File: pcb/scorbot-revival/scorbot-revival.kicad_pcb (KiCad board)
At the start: 2 copper layers, 3 parts, among them J1 DB-50, J2 Raspberry_Pi_2_3, U1 L293D

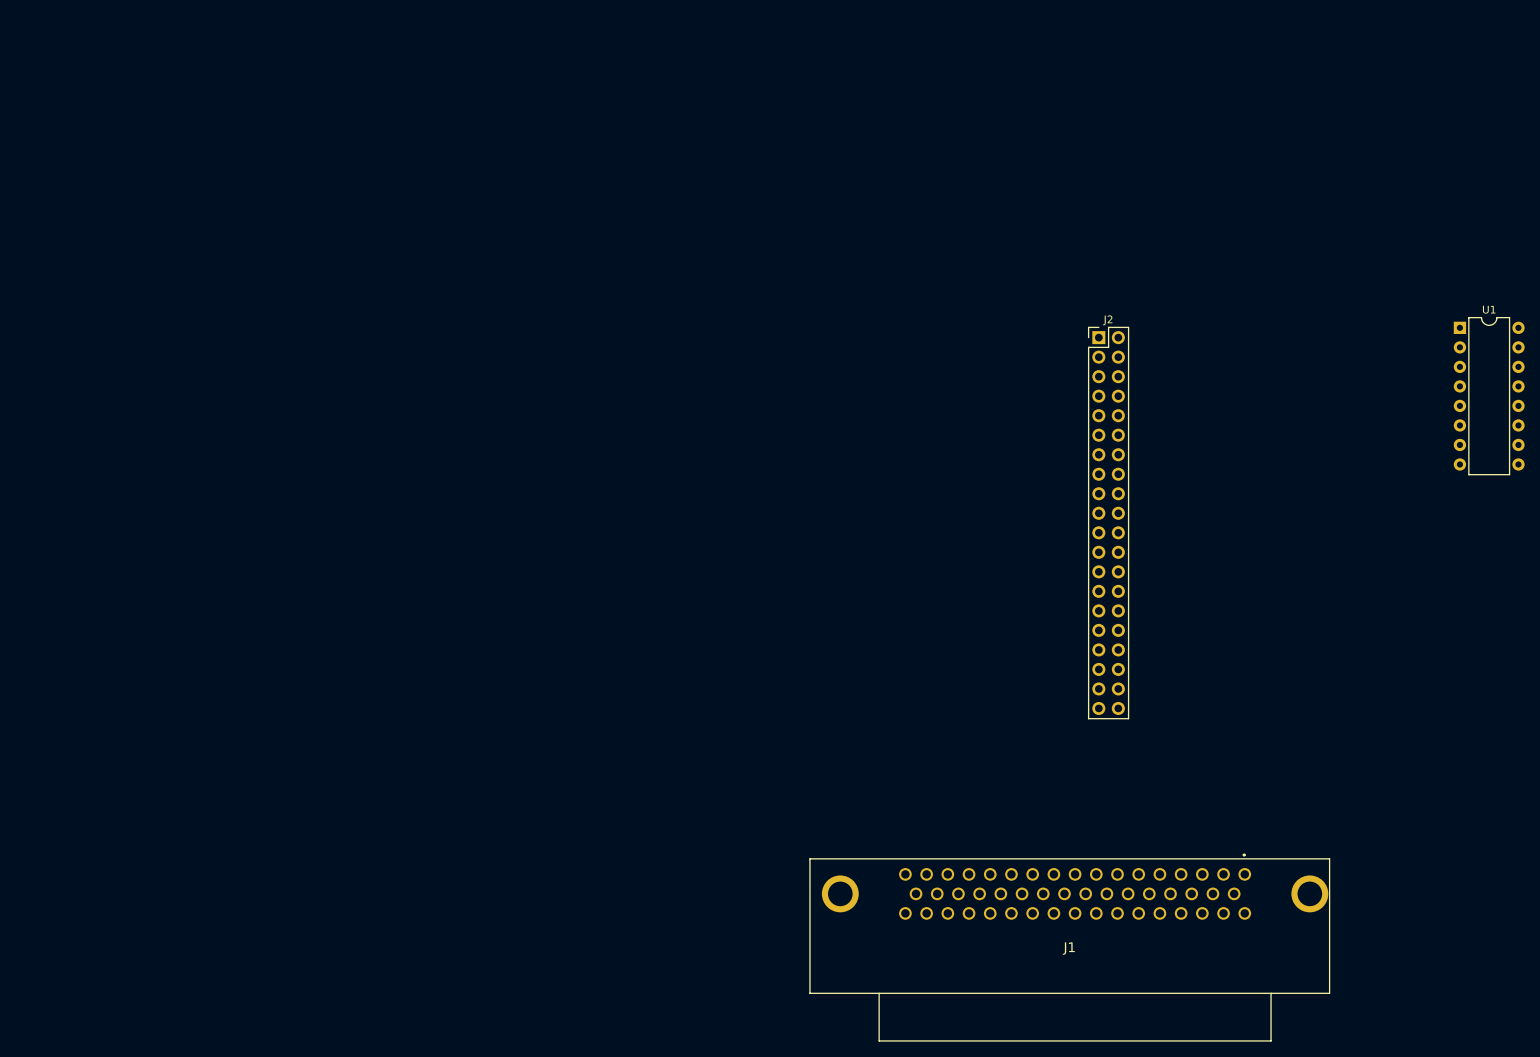
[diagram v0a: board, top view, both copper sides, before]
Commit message: [pcb] added labels to DB50 connector in schematic
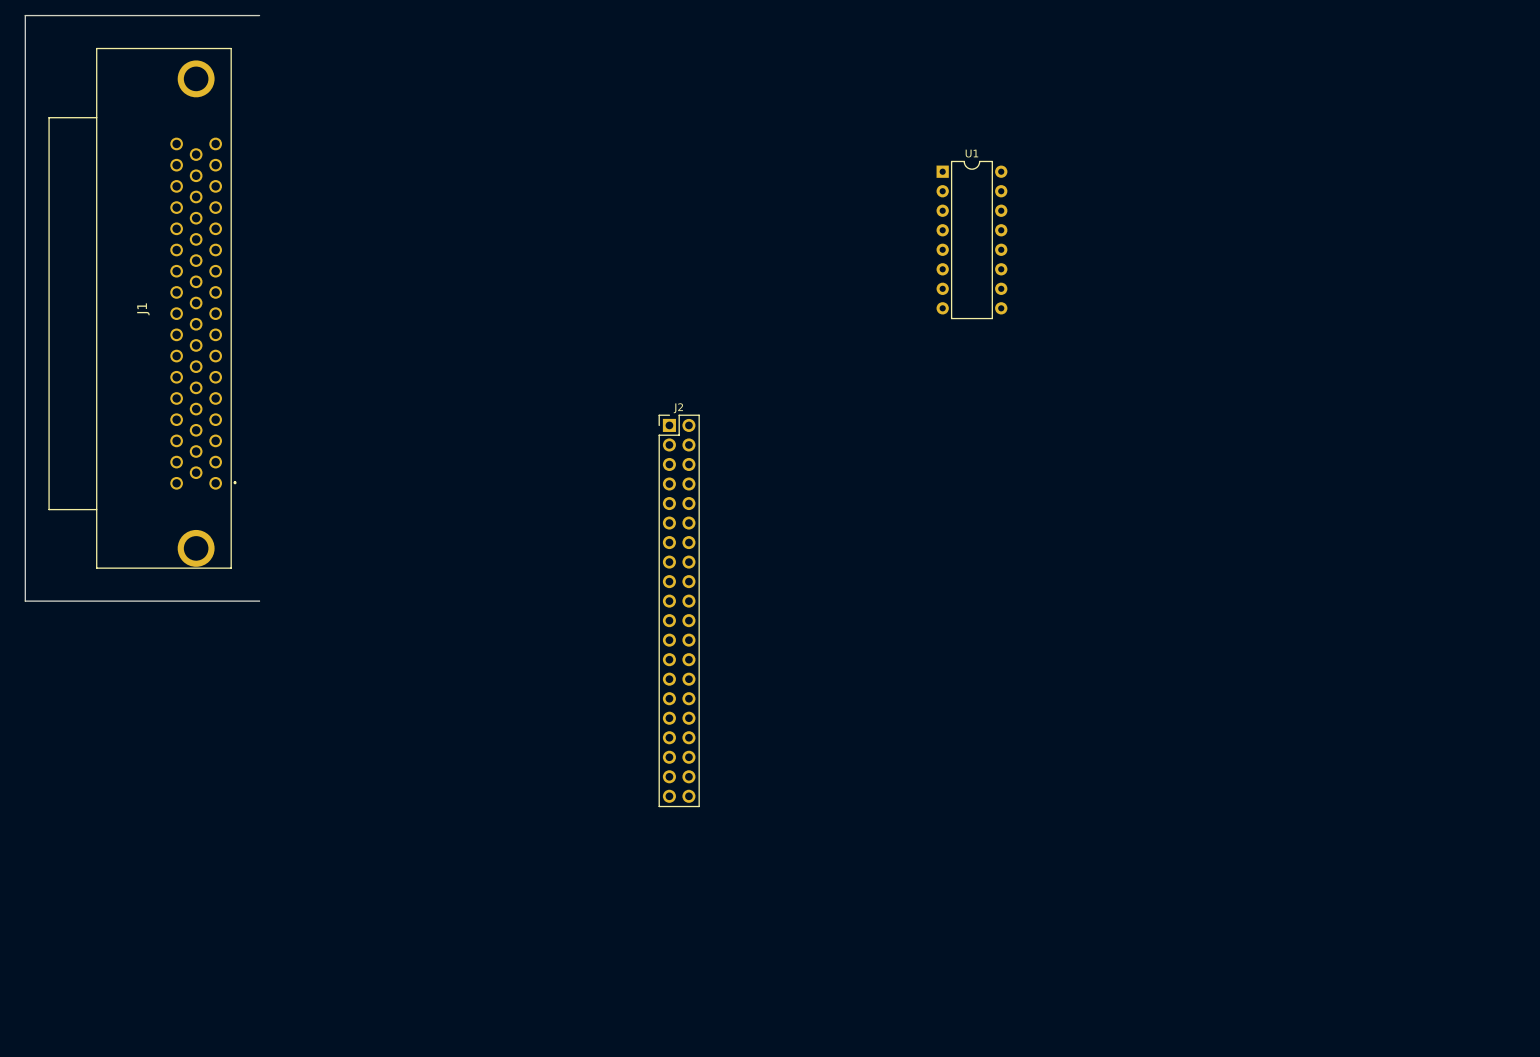
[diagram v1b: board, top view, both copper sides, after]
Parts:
- moved J1 146.6 mm to (35.6, 53.3), turned to 270 degrees
- moved U1 70.3 mm to (139.7, 35.6)
- moved J2 57.0 mm to (104.1, 68.6)
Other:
- board outline added: 30.5 x 76.2 mm

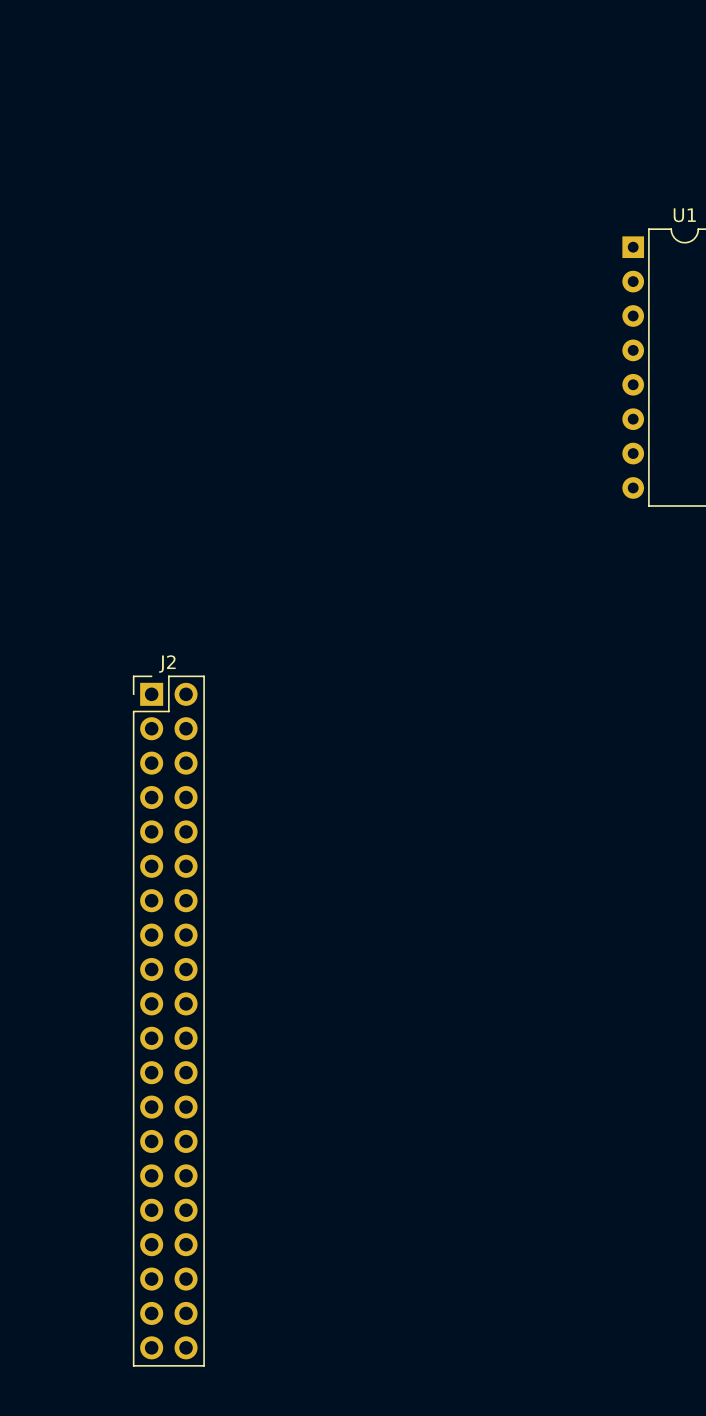
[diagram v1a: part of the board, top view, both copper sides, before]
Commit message: [pcb] add PIC16CE625-04I to schematic + pcbnew
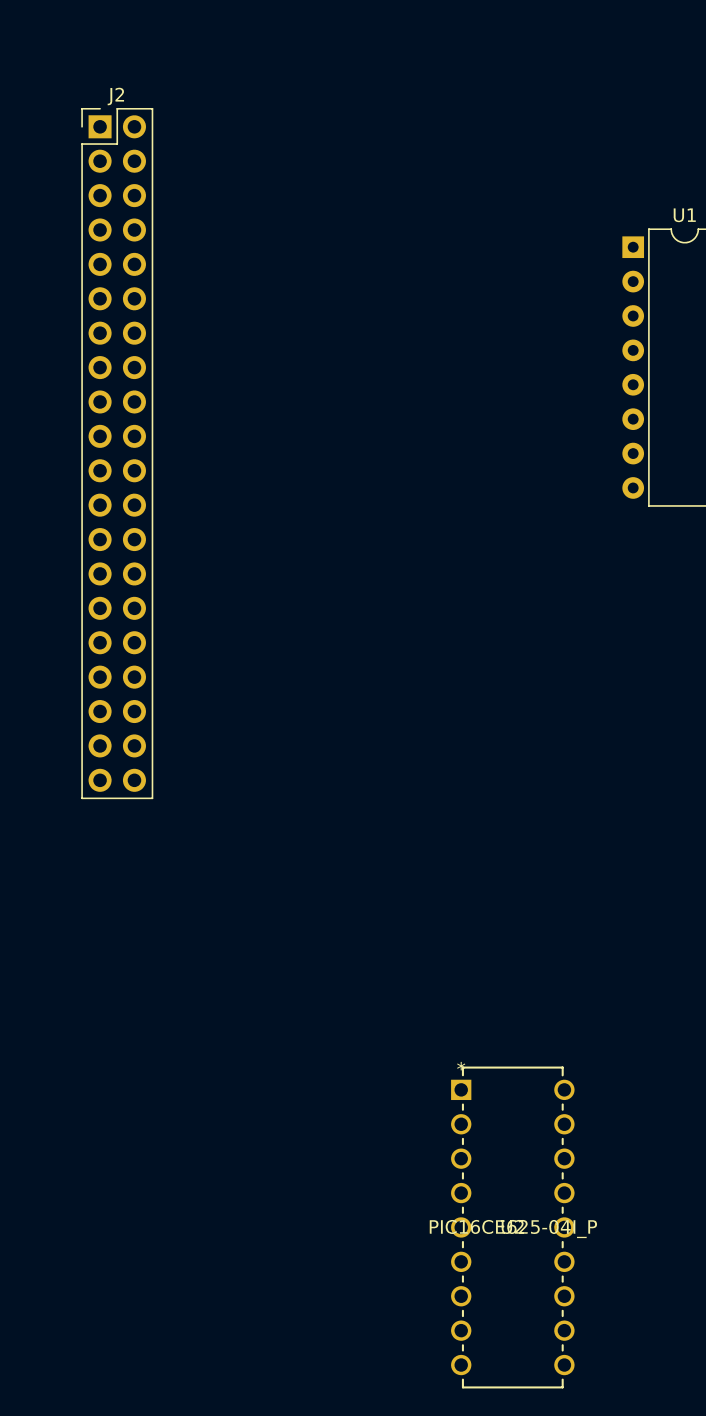
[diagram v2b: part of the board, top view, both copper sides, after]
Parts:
- added U2: PIC16CE625-04I_P, PIC16CE625-04I/P:PIC16CE625-04I&slash_P, F.Cu at (134.6, 118.1)
- moved J2 42.1 mm to (100.3, 26.7)
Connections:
- net Net-(J1-Pad1) renamed /M2_LOGIC_P0
- net Net-(J1-Pad10) renamed /M3_LOGIC_LED
- net Net-(J1-Pad11) renamed /M1_LOGIC_LED
- net Net-(J1-Pad12) renamed /Grp+
- net Net-(J1-Pad13) renamed /M5+
- net Net-(J1-Pad14) renamed /M4+
- net Net-(J1-Pad15) renamed /M3+
- net Net-(J1-Pad16) renamed /M2+
- net Net-(J1-Pad17) renamed /M1+
- net Net-(J1-Pad18) renamed /M5_LOGIC_P0
- net Net-(J1-Pad19) renamed /Grp_LOGIC_P1
- net Net-(J1-Pad2) renamed /M1_LOGIC_P0
- net Net-(J1-Pad20) renamed /M4_LOGIC_P1
- net Net-(J1-Pad21) renamed /M2_LOGIC_P1
- net Net-(J1-Pad22) renamed /Grp_LOGIC_MS
- net Net-(J1-Pad23) renamed /M1_LOGIC_MS
- net Net-(J1-Pad24) renamed /M3_LOGIC_MS
- net Net-(J1-Pad25) renamed /Grp_LOGIC_LED
- net Net-(J1-Pad26) renamed /M4_LOGIC_LED
- net Net-(J1-Pad27) renamed /M2_LOGIC_LED
- net Net-(J1-Pad3) renamed /M5_LOGIC_P1
- net Net-(J1-Pad34) renamed /Grp_LOGIC_P0
- net Net-(J1-Pad35) renamed /M4_LOGIC_P0
- net Net-(J1-Pad36) renamed /M3_LOGIC_P0
- net Net-(J1-Pad4) renamed /M3_LOGIC_P1
- net Net-(J1-Pad45) renamed /Grp-
- net Net-(J1-Pad46) renamed /M5-
- net Net-(J1-Pad47) renamed /M4-
- net Net-(J1-Pad48) renamed /M3-
- net Net-(J1-Pad49) renamed /M2-
- net Net-(J1-Pad5) renamed /M1_LOGIC_P1
- net Net-(J1-Pad50) renamed /M1-
- net Net-(J1-Pad6) renamed /M5_LOGIC_MS
- net Net-(J1-Pad7) renamed /M2_LOGIC_MS
- net Net-(J1-Pad8) renamed /M4_LOGIC_MS
- net Net-(J1-Pad9) renamed /M5_LOGIC_LED
- J1 pad 28: Net-(J1-Pad28) -> /Grp_LOGIC_GND
- J1 pad 29: Net-(J1-Pad29) -> /M5_LOGIC_GND
- J1 pad 30: Net-(J1-Pad30) -> /M4_LOGIC_GND
- J1 pad 31: Net-(J1-Pad31) -> /M3_LOGIC_GND
- J1 pad 32: Net-(J1-Pad32) -> /M2_LOGIC_GND
- J1 pad 33: Net-(J1-Pad33) -> /M1_LOGIC_GND
- J2 pad 14: Net-(J2-Pad14) -> /M3_LOGIC_GND
- J2 pad 20: Net-(J2-Pad20) -> /M4_LOGIC_GND
- J2 pad 25: Net-(J2-Pad25) -> /M5_LOGIC_GND
- J2 pad 30: Net-(J2-Pad30) -> /Grp_LOGIC_GND
- J2 pad 6: Net-(J2-Pad6) -> /M1_LOGIC_GND
- J2 pad 9: Net-(J2-Pad9) -> /M2_LOGIC_GND

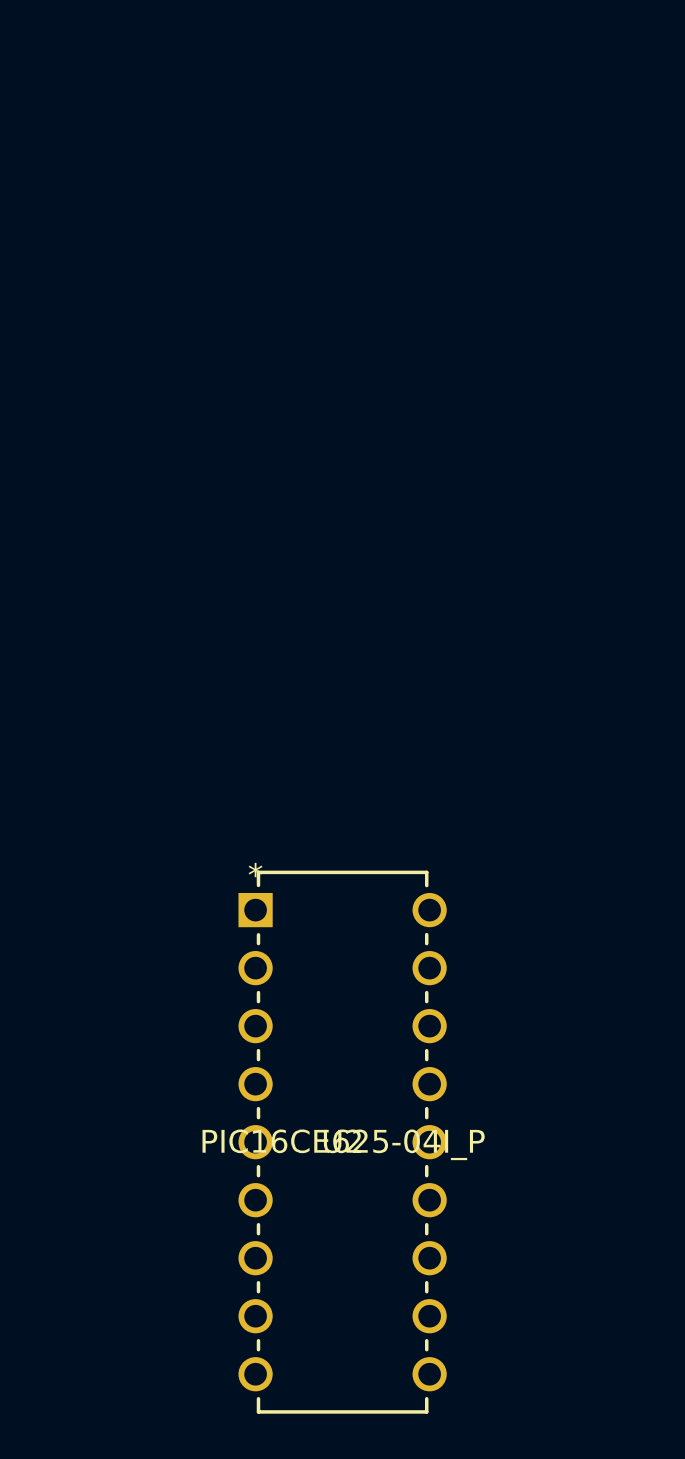
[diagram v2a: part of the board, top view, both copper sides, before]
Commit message: [pcb] replace old PIC with PIC18F2431-E_SP
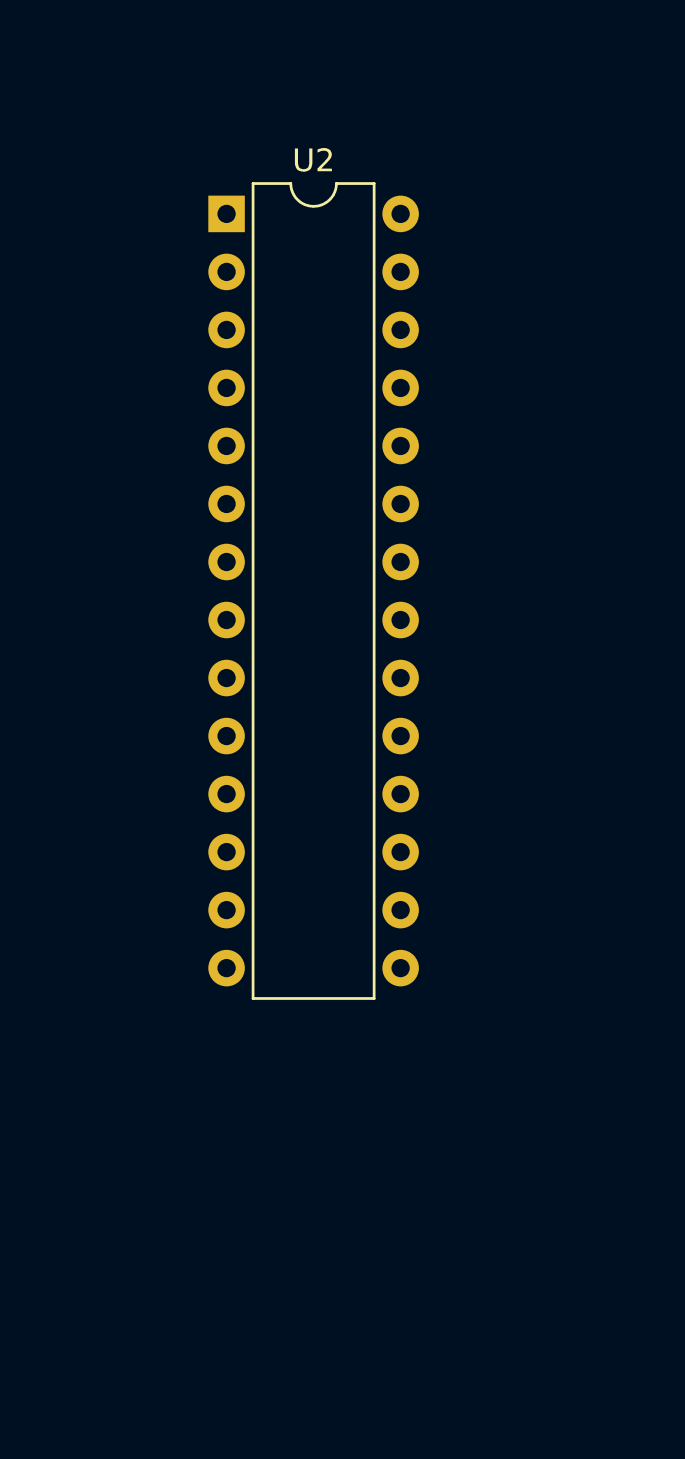
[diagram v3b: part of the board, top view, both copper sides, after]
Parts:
- U2: value PIC16CE625-04I_P -> PIC18F2431-E_SP; footprint PIC16CE625-04I/P:PIC16CE625-04I&slash_P -> Package_DIP:DIP-28_W7.62mm
- moved U2 51.6 mm to (125.7, 67.3)
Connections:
- J1 pad 1: /M2_LOGIC_P0 -> (no net)
- J1 pad 10: /M3_LOGIC_LED -> (no net)
- J1 pad 11: /M1_LOGIC_LED -> (no net)
- J1 pad 12: /Grp+ -> (no net)
- J1 pad 13: /M5+ -> (no net)
- J1 pad 14: /M4+ -> (no net)
- J1 pad 15: /M3+ -> (no net)
- J1 pad 16: /M2+ -> (no net)
- J1 pad 17: /M1+ -> (no net)
- J1 pad 18: /M5_LOGIC_P0 -> (no net)
- J1 pad 19: /Grp_LOGIC_P1 -> (no net)
- J1 pad 2: /M1_LOGIC_P0 -> (no net)
- J1 pad 20: /M4_LOGIC_P1 -> (no net)
- J1 pad 21: /M2_LOGIC_P1 -> (no net)
- J1 pad 22: /Grp_LOGIC_MS -> (no net)
- J1 pad 23: /M1_LOGIC_MS -> (no net)
- J1 pad 24: /M3_LOGIC_MS -> (no net)
- J1 pad 25: /Grp_LOGIC_LED -> (no net)
- J1 pad 26: /M4_LOGIC_LED -> (no net)
- J1 pad 27: /M2_LOGIC_LED -> (no net)
- J1 pad 3: /M5_LOGIC_P1 -> (no net)
- J1 pad 34: /Grp_LOGIC_P0 -> (no net)
- J1 pad 35: /M4_LOGIC_P0 -> (no net)
- J1 pad 36: /M3_LOGIC_P0 -> (no net)
- J1 pad 37: Net-(J1-Pad37) -> (no net)
- J1 pad 38: Net-(J1-Pad38) -> (no net)
- J1 pad 39: Net-(J1-Pad39) -> (no net)
- J1 pad 4: /M3_LOGIC_P1 -> (no net)
- J1 pad 40: Net-(J1-Pad40) -> (no net)
- J1 pad 41: Net-(J1-Pad41) -> (no net)
- J1 pad 42: Net-(J1-Pad42) -> (no net)
- J1 pad 43: Net-(J1-Pad43) -> (no net)
- J1 pad 44: Net-(J1-Pad44) -> (no net)
- J1 pad 45: /Grp- -> (no net)
- J1 pad 46: /M5- -> (no net)
- J1 pad 47: /M4- -> (no net)
- J1 pad 48: /M3- -> (no net)
- J1 pad 49: /M2- -> (no net)
- J1 pad 5: /M1_LOGIC_P1 -> (no net)
- J1 pad 50: /M1- -> (no net)
- J1 pad 6: /M5_LOGIC_MS -> (no net)
- J1 pad 7: /M2_LOGIC_MS -> (no net)
- J1 pad 8: /M4_LOGIC_MS -> (no net)
- J1 pad 9: /M5_LOGIC_LED -> (no net)
- J2 pad 1: Net-(J2-Pad1) -> (no net)
- J2 pad 10: Net-(J2-Pad10) -> (no net)
- J2 pad 11: Net-(J2-Pad11) -> (no net)
- J2 pad 12: Net-(J2-Pad12) -> (no net)
- J2 pad 13: Net-(J2-Pad13) -> (no net)
- J2 pad 15: Net-(J2-Pad15) -> (no net)
- J2 pad 16: Net-(J2-Pad16) -> (no net)
- J2 pad 17: Net-(J2-Pad17) -> (no net)
- J2 pad 18: Net-(J2-Pad18) -> (no net)
- J2 pad 19: Net-(J2-Pad19) -> (no net)
- J2 pad 2: Net-(J2-Pad2) -> (no net)
- J2 pad 21: Net-(J2-Pad21) -> (no net)
- J2 pad 22: Net-(J2-Pad22) -> (no net)
- J2 pad 23: Net-(J2-Pad23) -> (no net)
- J2 pad 24: Net-(J2-Pad24) -> (no net)
- J2 pad 26: Net-(J2-Pad26) -> (no net)
- J2 pad 27: Net-(J2-Pad27) -> (no net)
- J2 pad 28: Net-(J2-Pad28) -> (no net)
- J2 pad 29: Net-(J2-Pad29) -> (no net)
- J2 pad 3: Net-(J2-Pad3) -> (no net)
- J2 pad 31: Net-(J2-Pad31) -> (no net)
- J2 pad 32: Net-(J2-Pad32) -> (no net)
- J2 pad 33: Net-(J2-Pad33) -> (no net)
- J2 pad 34: Net-(J2-Pad34) -> (no net)
- J2 pad 35: Net-(J2-Pad35) -> (no net)
- J2 pad 36: Net-(J2-Pad36) -> (no net)
- J2 pad 37: Net-(J2-Pad37) -> (no net)
- J2 pad 38: Net-(J2-Pad38) -> (no net)
- J2 pad 39: Net-(J2-Pad39) -> (no net)
- J2 pad 4: Net-(J2-Pad4) -> (no net)
- J2 pad 40: Net-(J2-Pad40) -> (no net)
- J2 pad 5: Net-(J2-Pad5) -> (no net)
- J2 pad 7: Net-(J2-Pad7) -> (no net)
- J2 pad 8: Net-(J2-Pad8) -> (no net)
- U1 pad 1: Net-(U1-Pad1) -> (no net)
- U1 pad 10: Net-(U1-Pad10) -> (no net)
- U1 pad 11: Net-(U1-Pad11) -> (no net)
- U1 pad 12: Net-(U1-Pad12) -> (no net)
- U1 pad 13: Net-(U1-Pad13) -> (no net)
- U1 pad 14: Net-(U1-Pad14) -> (no net)
- U1 pad 15: Net-(U1-Pad15) -> (no net)
- U1 pad 16: Net-(U1-Pad16) -> (no net)
- U1 pad 2: Net-(U1-Pad2) -> (no net)
- U1 pad 3: Net-(U1-Pad3) -> (no net)
- U1 pad 4: Net-(U1-Pad4) -> (no net)
- U1 pad 5: Net-(U1-Pad5) -> (no net)
- U1 pad 6: Net-(U1-Pad6) -> (no net)
- U1 pad 7: Net-(U1-Pad7) -> (no net)
- U1 pad 8: Net-(U1-Pad8) -> (no net)
- U1 pad 9: Net-(U1-Pad9) -> (no net)
- U2 pad 1: Net-(U2-Pad1) -> (no net)
- U2 pad 10: Net-(U2-Pad10) -> (no net)
- U2 pad 11: Net-(U2-Pad11) -> (no net)
- U2 pad 12: Net-(U2-Pad12) -> (no net)
- U2 pad 13: Net-(U2-Pad13) -> (no net)
- U2 pad 14: Net-(U2-Pad14) -> (no net)
- U2 pad 15: Net-(U2-Pad15) -> (no net)
- U2 pad 16: Net-(U2-Pad16) -> (no net)
- U2 pad 17: Net-(U2-Pad17) -> (no net)
- U2 pad 18: Net-(U2-Pad18) -> (no net)
- U2 pad 2: Net-(U2-Pad2) -> (no net)
- U2 pad 3: Net-(U2-Pad3) -> (no net)
- U2 pad 4: Net-(U2-Pad4) -> (no net)
- U2 pad 5: Net-(U2-Pad5) -> (no net)
- U2 pad 6: Net-(U2-Pad6) -> (no net)
- U2 pad 7: Net-(U2-Pad7) -> (no net)
- U2 pad 8: Net-(U2-Pad8) -> (no net)
- U2 pad 9: Net-(U2-Pad9) -> (no net)
